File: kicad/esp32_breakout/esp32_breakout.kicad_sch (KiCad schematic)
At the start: 30 parts, among them J1 JST PH F, J10 JST PH F, J11 JST PH F, J2 JST PH F, J3 JST PH F, J4 DC-005 5.5x2.1mm, J5 Deans T-Plug M, J6 Header F, J7 Header F, J8 Header F, J9 JST PH F, Q1 BSS123, SW1 SS12D10, U1 ESP32 DEV KIT 30-pin, U2 Mini560-Pro

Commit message: PCB updated to product
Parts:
- removed D1: CGRA4004-G, Diode_SMD:D_SMA, symbol Device:D
- removed J11: JST PH F, Connector_JST:JST_PH_B6B-PH-K_1x06_P2.00mm_Vertical, symbol Connector_Generic:Conn_01x06
- removed J4: DC-005 5.5x2.1mm, Connector_BarrelJack:BarrelJack_GCT_DCJ200-10-A_Horizontal, symbol Connector:Barrel_Jack_Switch
- removed J5: Deans T-Plug M, Makerspet:DEANS-T-PLUG, symbol Makerspet:Deans T-Plug
- removed J6: Header F, Connector_PinHeader_2.54mm:PinHeader_2x04_P2.54mm_Vertical, symbol Connector_Generic:Conn_02x04_Top_Bottom
- removed J8: Header F, Connector_PinHeader_2.54mm:PinHeader_1x03_P2.54mm_Vertical, symbol Connector_Generic:Conn_01x03
- removed Q1: BSS123, Package_TO_SOT_SMD:SOT-23, symbol Transistor_FET:BSS123
- removed R5: 1k, Resistor_SMD:R_0603_1608Metric, symbol Device:R_Small_US
- removed R6: 10k, Resistor_SMD:R_0603_1608Metric, symbol Device:R_Small_US
- removed U2: Mini560-Pro, Makerspet:Mini560-Pro, symbol Makerspet:DC-DC
- added D2: FS26, Diode_SMD:D_SOD-123F, symbol Device:D_Schottky
- added F1: FCC20202AATP, Fuse:Fuse_0805_2012Metric, symbol Device:Fuse
- added J4: XT30U-M, Connector_AMASS:AMASS_XT30U-M_1x02_P5.0mm_Vertical, symbol Makerspet:XT30UPB-M
- added J5: Header F 2.54mm, Connector_PinHeader_2.54mm:PinHeader_1x08_P2.54mm_Vertical, symbol Connector_Generic:Conn_01x08
- added U2: LM2596 Module, Makerspet:LM2596 Module, symbol Makerspet:DC-DC Module
- J6: renamed from J7; value Header F -> Header F 2.54mm
- R10: value 4.7k -> 10k
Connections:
- net +24V: now also U2.4 (VIN+)
- net +3V3: now also R1.1, R2.1, J5.2 (Pin_2)
- net +5V: now also J5.1 (Pin_1), U2.3 (VOUT+)
- net GND: now also J4.1 (-), J5.8 (Pin_8), U2.1 (VIN-), U2.2 (VOUT-); no longer R1.2, R2.2
- net GPIO26_TOUCH: now also J5.5 (Pin_5)
- net GPIO27_TOUCH: now also J5.4 (Pin_4)
- net GPIO32_TOUCH: now also J5.3 (Pin_3)
- net GPIO4_TOUCH: now also J5.6 (Pin_6)
- net GPIO5_BOOT_STRAP: now also J5.7 (Pin_7)
- net I2C_INT: now also R2.2
- net I2C_SCL: now also R1.2
- net MOT_PWM_LEFT: no longer R1.1
- net MOT_PWM_RIGHT: no longer R2.1
- net +BATT: no longer names the net of SW1.1 (A)
- net +BATT: now also D2.1 (K)
- new net: F1.1, J4.2 (+)
- new net: D2.2 (A), F1.2
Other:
- note added: "BATTERY Input voltage 24V Max 24V input current approx. 2.2A with both motors stalled Safety - 24V input/output overcurrent protection using a 2A fuse - 24V input reverse polarity protection using a Schottki diode - input overvoltage LM2596 40V max; motors not protected - 5V output LM2596 provides current limit, short, thermal protection"
- note added: "LASER DISTANCE SENSOR YDLidar X4, https://www.ydlidar.com/ Connector pinout VCC 5V TX all I/O 3.3V RX GND M_SCTR speed DEV_EN N/C M_EN N/C"
- note added: "MOTORS CHR-GM25-BLDC2418 i45 Type BLDC Voltage 24V, I/O 5V Diameter 25mm, weight 69g Max RPM 200, rated RPM 145 Rated torque 1.5Kg*cm, stall torque 5Kg*cm Max power 2.5W, stall current 0.65A https://www.aliexpress.us/item/2251832633601682.html"
- note added: "SONAR US-100"
- note added: "VCC 5V Trig/Tx Echo/Rx GND GND"
- note removed: "BATTERY"
- note removed: "Changing: MOT_FG_RIGHT from GPIO27 to GPIO35_IN LDS_MOT_EN from GPIO12_OUT to GPIO19 MOT_CW_LEFT from GPIO32 to GPIO23"
- note removed: "LASER POINTER"
- note removed: "Laser Distance Sensor YDLidar X4 VCC 5V TX all I/O 3.3V RX GND M_SCTR speed DEV_EN N/C M_EN N/C https://www.ydlidar.com/"
- note removed: "Motors CHR-GM25-BLDC2418 Type BLDC Voltage 24V, I/O 5V Diameter 25mm Weight 69g Rated RPM 190 Rated torque 1.1Kg*cm Max power 2.5W Stall torque 3.5Kg*cm Stall current 0.35A https://www.aliexpress.us/item/2251832633601682.html"
- note removed: "SONAR"
- moved on the sheet: J10, J6, J9, R10, R7, R8, R9, SW1

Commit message: Pico head WiP
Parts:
- J1, J2: value JST PH F -> JST B5B-PH-K-S
- J10, J9: value JST PH F -> JST B6B-PH-K-S
- J3: value JST PH F -> JST B7B-PH-K-S
- J5: value Header F 2.54mm -> HDR F 2.54MM VERT
- J6: value Header F 2.54mm -> HDR F 2.54MM 5-pin VERT
- U1: value ESP32 DEV KIT 30-pin -> ESP32 DEV KIT Module 30-pin
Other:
- note added: "LASER DISTANCE SENSOR YDLidar X4, https://www.ydlidar.com/ YDLidar X4 connector pinout: VCC 5V TX all I/O 3.3V RX GND M_SCTR speed DEV_EN N/C M_EN N/C"
- note removed: "LASER DISTANCE SENSOR YDLidar X4, https://www.ydlidar.com/ Connector pinout VCC 5V TX all I/O 3.3V RX GND M_SCTR speed DEV_EN N/C M_EN N/C"
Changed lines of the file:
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@@
     (effects (font (size 1.27 1.27)) (justify left bottom))
   )
-  (text "LASER DISTANCE SENSOR\n\nYDLidar X4, https://www.ydlidar.com/\n\nConnector pinout\nVCC 5V\nTX all I/O 3.3V\nRX\nGND\nM_SCTR speed\nDEV_EN N/C\nM_EN\nN/C"
+  (text "LASER DISTANCE SENSOR\n\nYDLidar X4, https://www.ydlidar.com/\nYDLidar X4 connector pinout:\nVCC 5V\nTX all I/O 3.3V\nRX\nGND\nM_SCTR speed\nDEV_EN N/C\nM_EN\nN/C"
     (at 82.042 124.46 0)
     (effects (font (size 1.27 1.27)) (justify left bottom))
@@
     (effects (font (size 1.27 1.27)) (justify left bottom))
   )
-  (label "LDS_TX" (at 109.728 139.446 0) (fields_autoplaced)
+  (label "LDS_TX" (at 105.156 139.446 0) (fields_autoplaced)
     (effects (font (size 1.27 1.27)) (justify left bottom))
   )
@@
     (effects (font (size 1.27 1.27)) (justify left bottom))
   )
-  (label "LDS_MOT_PWM" (at 109.728 147.066 0) (fields_autoplaced)
+  (label "LDS_MOT_PWM" (at 105.156 147.066 0) (fields_autoplaced)
     (effects (font (size 1.27 1.27)) (justify left bottom))
   )
@@
     (effects (font (size 1.27 1.27)) (justify left bottom))
   )
-  (label "LDS_RX" (at 109.728 141.986 0) (fields_autoplaced)
+  (label "LDS_RX" (at 105.156 141.986 0) (fields_autoplaced)
     (effects (font (size 1.27 1.27)) (justify left bottom))
   )
@@
     (effects (font (size 1.27 1.27)) (justify left bottom))
   )
-  (label "LDS_MOT_EN" (at 109.728 152.146 0) (fields_autoplaced)
+  (label "LDS_MOT_EN" (at 105.156 152.146 0) (fields_autoplaced)
     (effects (font (size 1.27 1.27)) (justify left bottom))
   )
@@
       (effects (font (size 1.27 1.27)) (justify left))
     )
-    (property "Value" "JST PH F" (at 252.349 75.819 0)
+    (property "Value" "JST B6B-PH-K-S" (at 260.35 74.93 90)
       (effects (font (size 1.27 1.27)) (justify left))
     )
@@
   (symbol (lib_id "Connector_Generic:Conn_01x05") (at 29.21 139.065 0) (mirror y) (unit 1)
     (in_bom yes) (on_board yes) (dnp no)
-    (property "Reference" "J2" (at 29.21 128.905 0)
-      (effects (font (size 1.27 1.27)))
-    )
-    (property "Value" "JST PH F" (at 30.48 131.445 0)
+    (property "Reference" "J2" (at 29.21 130.556 0)
+      (effects (font (size 1.27 1.27)))
+    )
+    (property "Value" "JST B5B-PH-K-S" (at 26.162 139.192 90)
       (effects (font (size 1.27 1.27)))
     )
@@
   (symbol (lib_id "Connector_Generic:Conn_01x07") (at 94.488 144.526 0) (mirror y) (unit 1)
     (in_bom yes) (on_board yes) (dnp no)
-    (property "Reference" "J3" (at 94.488 131.191 0)
-      (effects (font (size 1.27 1.27)))
-    )
-    (property "Value" "JST PH F" (at 96.393 133.731 0)
+    (property "Reference" "J3" (at 94.488 133.35 0)
+      (effects (font (size 1.27 1.27)))
+    )
+    (property "Value" "JST B7B-PH-K-S" (at 90.932 144.526 90)
       (effects (font (size 1.27 1.27)))
     )
@@
       (effects (font (size 1.27 1.27)) (justify left))
     )
-    (property "Value" "Header F 2.54mm" (at 188.722 48.006 0)
+    (property "Value" "HDR F 2.54MM VERT" (at 202.692 44.45 90)
       (effects (font (size 1.27 1.27)) (justify left))
     )
@@
   (symbol (lib_id "Makerspet:ESP32-DOIT-V1") (at 88.265 54.61 0) (unit 1)
     (in_bom yes) (on_board yes) (dnp no)
-    (property "Reference" "U1" (at 86.995 33.02 0)
-      (effects (font (size 1.27 1.27)))
-    )
-    (property "Value" "ESP32 DEV KIT 30-pin" (at 86.995 30.48 0)
+    (property "Reference" "U1" (at 87.122 32.258 0)
+      (effects (font (size 1.27 1.27)))
+    )
+    (property "Value" "ESP32 DEV KIT Module 30-pin" (at 87.122 77.47 0)
       (effects (font (size 1.27 1.27)))
     )
@@
       (effects (font (size 1.27 1.27)) (justify left))
     )
-    (property "Value" "Header F 2.54mm" (at 188.214 85.852 0)
+    (property "Value" "HDR F 2.54MM 5-pin VERT" (at 195.834 89.408 90)
       (effects (font (size 1.27 1.27)) (justify left))
     )
@@
   (symbol (lib_id "Makerspet:XT30UPB-M") (at 147.066 119.38 0) (unit 1)
     (in_bom yes) (on_board yes) (dnp no)
-    (property "Reference" "J4" (at 147.066 119.38 0)
-      (effects (font (size 1.27 1.27)))
-    )
-    (property "Value" "XT30U-M" (at 147.574 134.112 0)
+    (property "Reference" "J4" (at 147.066 120.396 0)
+      (effects (font (size 1.27 1.27)))
+    )
+    (property "Value" "XT30U-M" (at 141.224 126.746 90)
       (effects (font (size 1.27 1.27)))
     )
@@
   (symbol (lib_id "Connector_Generic:Conn_01x05") (at 28.575 174.625 0) (mirror y) (unit 1)
     (in_bom yes) (on_board yes) (dnp no)
-    (property "Reference" "J1" (at 28.575 164.465 0)
-      (effects (font (size 1.27 1.27)))
-    )
-    (property "Value" "JST PH F" (at 29.21 167.005 0)
+    (property "Reference" "J1" (at 28.702 166.37 0)
+      (effects (font (size 1.27 1.27)))
+    )
+    (property "Value" "JST B5B-PH-K-S" (at 25.4 175.006 90)
       (effects (font (size 1.27 1.27)))
     )
@@
       (effects (font (size 1.27 1.27)) (justify left))
     )
-    (property "Value" "JST PH F" (at 252.349 52.959 0)
-      (effects (font (size 1.27 1.27)) (justify left))
-    )
+    (property "Value" "JST B6B-PH-K-S" (at 260.35 51.308 90)
+      (effects (font (size 1.27 1.27)) (justify left))
+    )

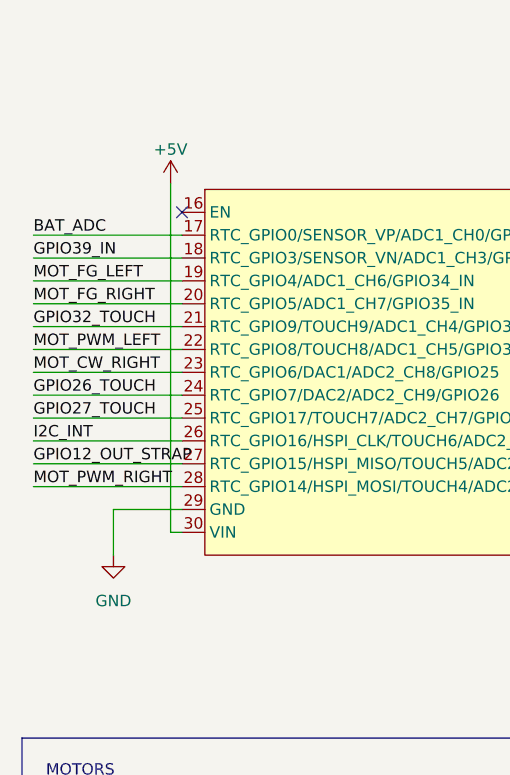
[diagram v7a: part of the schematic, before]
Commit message: 5V OR Schottky diode
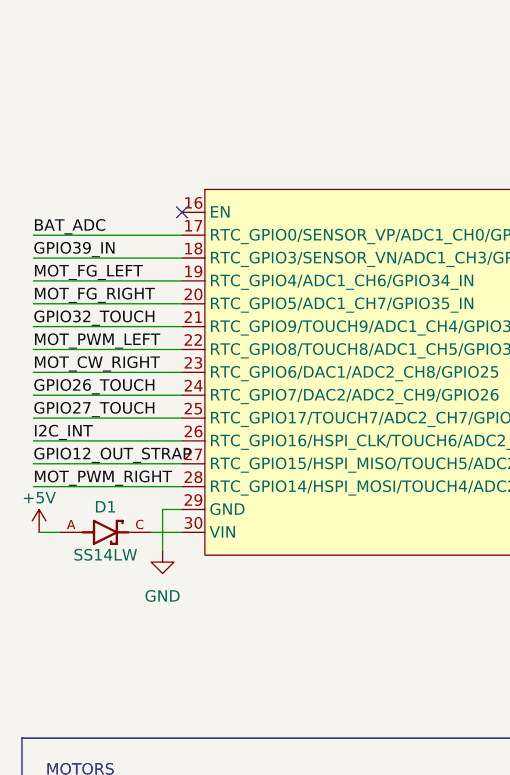
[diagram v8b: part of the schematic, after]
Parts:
- added D1: SS14LW, SS14LW:DIO_SS14LW, symbol Makerspet:SS14LW
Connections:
- net +5V: now also D1.A; no longer U1.30 (VIN)
- new net: D1.C, U1.30 (VIN)
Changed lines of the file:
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@@
     (stroke (width 0) (type default))
   )
-  (wire (pts (xy 32.385 69.85) (xy 24.765 69.85))
-    (stroke (width 0) (type default))
-  )
-  (wire (pts (xy 31.115 72.39) (xy 32.385 72.39))
+  (wire (pts (xy 32.385 69.85) (xy 30.226 69.85))
     (stroke (width 0) (type default))
   )
@@
     (stroke (width 0) (type default))
   )
+  (wire (pts (xy 18.796 72.39) (xy 16.51 72.39))
+    (stroke (width 0) (type default))
+  )
   (wire (pts (xy 99.568 141.986) (xy 116.713 141.986))
     (stroke (width 0) (type default))
@@
     (stroke (width 0) (type default))
   )
-  (wire (pts (xy 31.115 33.655) (xy 31.115 72.39))
-    (stroke (width 0) (type default))
-  )
   (wire (pts (xy 37.465 130.81) (xy 37.465 144.145))
     (stroke (width 0) (type default))
@@
     (stroke (width 0) (type default))
   )
+  (wire (pts (xy 28.956 72.39) (xy 32.385 72.39))
+    (stroke (width 0) (type default))
+  )
   (wire (pts (xy 251.714 37.084) (xy 245.364 37.084))
     (stroke (width 0) (type default))
@@
     (stroke (width 0) (type default))
   )
-  (wire (pts (xy 24.765 69.85) (xy 24.765 74.93))
+  (wire (pts (xy 30.226 69.85) (xy 30.226 74.422))
     (stroke (width 0) (type default))
   )
@@
     )
   )
-  (symbol (lib_id "power:+5V") (at 31.115 33.655 0) (unit 1)
-    (in_bom yes) (on_board yes) (dnp no) (fields_autoplaced)
-    (property "Reference" "#PWR02" (at 31.115 37.465 0)
-      (effects (font (size 1.27 1.27)) hide)
-    )
-    (property "Value" "+5V" (at 31.115 29.845 0)
-      (effects (font (size 1.27 1.27)))
-    )
-    (property "Footprint" "" (at 31.115 33.655 0)
-      (effects (font (size 1.27 1.27)) hide)
-    )
-    (property "Datasheet" "" (at 31.115 33.655 0)
+  (symbol (lib_id "power:+5V") (at 16.51 72.39 0) (unit 1)
+    (in_bom yes) (on_board yes) (dnp no) (fields_autoplaced)
+    (property "Reference" "#PWR02" (at 16.51 76.2 0)
+      (effects (font (size 1.27 1.27)) hide)
+    )
+    (property "Value" "+5V" (at 16.51 68.58 0)
+      (effects (font (size 1.27 1.27)))
+    )
+    (property "Footprint" "" (at 16.51 72.39 0)
+      (effects (font (size 1.27 1.27)) hide)
+    )
+    (property "Datasheet" "" (at 16.51 72.39 0)
       (effects (font (size 1.27 1.27)) hide)
     )
@@
         (path "/e24ae185-8f18-408c-aee8-f727519bade3"
           (reference "R4") (unit 1)
+        )
+      )
+    )
+  )
+  (symbol (lib_id "Makerspet:SS14LW") (at 23.876 72.39 0) (unit 1)
+    (in_bom yes) (on_board yes) (dnp no)
+    (property "Reference" "D1" (at 23.876 69.596 0)
+      (effects (font (size 1.27 1.27)))
+    )
+    (property "Value" "SS14LW" (at 23.876 74.93 0)
+      (effects (font (size 1.27 1.27)))
+    )
+    (property "Footprint" "SS14LW:DIO_SS14LW" (at 23.876 78.74 0)
+      (effects (font (size 1.27 1.27)) (justify bottom) hide)
+    )
+    (property "Datasheet" "" (at 23.876 72.39 0)
+      (effects (font (size 1.27 1.27)) hide)
+    )
+    (pin "A")
+    (pin "C")
+    (instances
+      (project "esp32_breakout"
+        (path "/e24ae185-8f18-408c-aee8-f727519bade3"
+          (reference "D1") (unit 1)
         )
       )
@@
     )
   )
-  (symbol (lib_id "power:GND") (at 24.765 74.93 0) (unit 1)
-    (in_bom yes) (on_board yes) (dnp no) (fields_autoplaced)
-    (property "Reference" "#PWR01" (at 24.765 81.28 0)
-      (effects (font (size 1.27 1.27)) hide)
-    )
-    (property "Value" "GND" (at 24.765 80.01 0)
-      (effects (font (size 1.27 1.27)))
-    )
-    (property "Footprint" "" (at 24.765 74.93 0)
-      (effects (font (size 1.27 1.27)) hide)
-    )
-    (property "Datasheet" "" (at 24.765 74.93 0)
-      (effects (font (size 1.27 1.27)) hide)
-    )
+  (symbol (lib_id "power:GND") (at 30.226 74.422 0) (unit 1)
+    (in_bom yes) (on_board yes) (dnp no) (fields_autoplaced)
+    (property "Reference" "#PWR01" (at 30.226 80.772 0)
+      (effects (font (size 1.27 1.27)) hide)
+    )
+    (property "Value" "GND" (at 30.226 79.502 0)
+      (effects (font (size 1.27 1.27)))
+    )
+    (property "Footprint" "" (at 30.226 74.422 0)
+      (effects (font (size 1.27 1.27)) hide)
+    )
+    (property "Datasheet" "" (at 30.226 74.422 0)
+      (effects (font (size 1.27 1.27)) hide)
+    )
